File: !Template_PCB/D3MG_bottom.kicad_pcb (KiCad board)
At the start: 2 copper layers, 50 x 86.5 mm, 0 parts

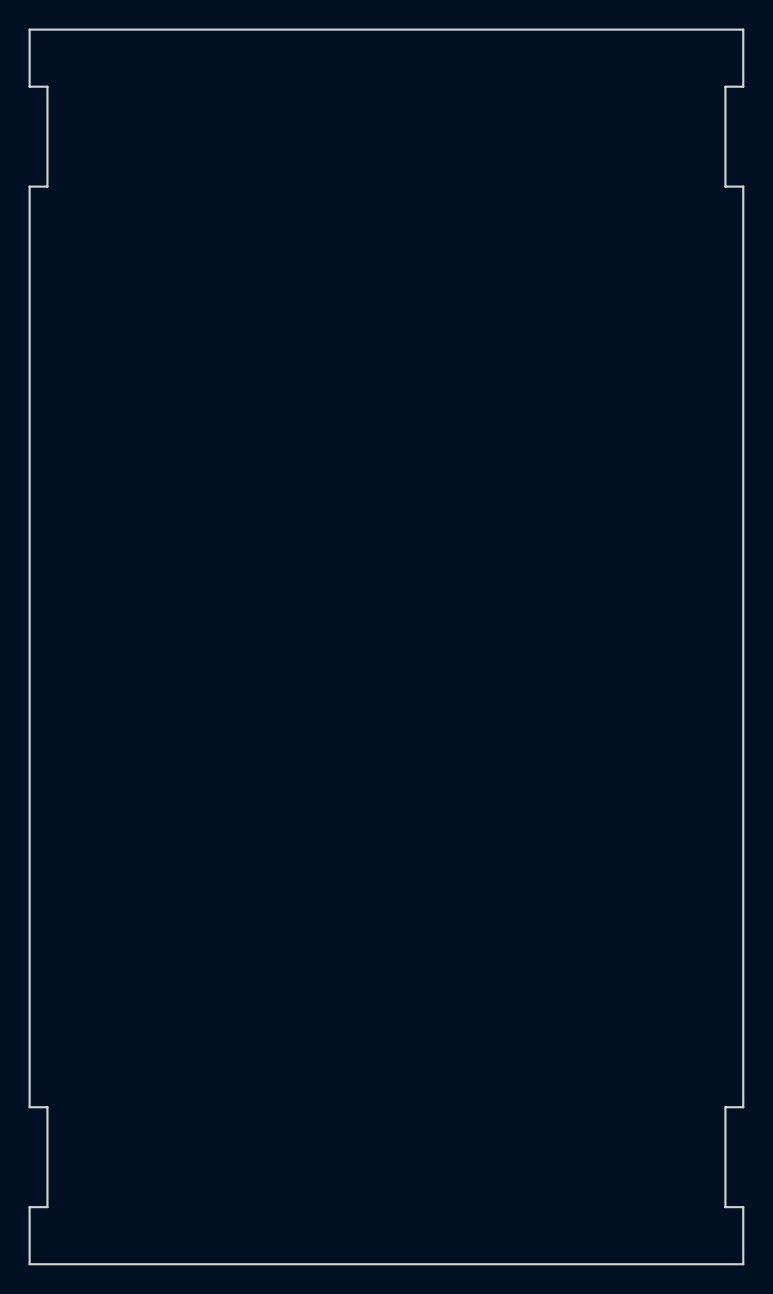
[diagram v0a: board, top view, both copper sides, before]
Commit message: + Spruce_60x70 Template_PCB
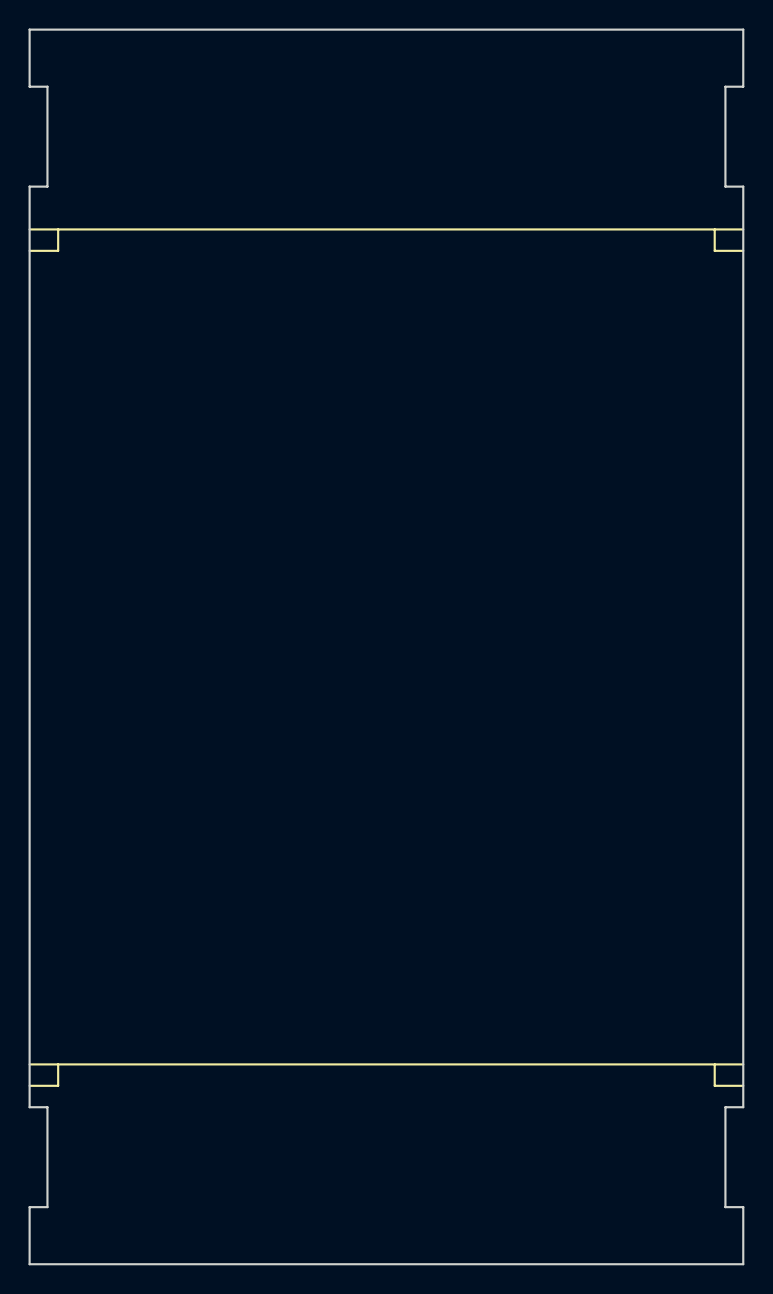
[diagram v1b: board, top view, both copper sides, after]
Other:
- board text removed: "bottom"
- board text removed: "top"
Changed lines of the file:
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@@
     (area 99.924999 49.924999 150.075001 136.575001)
     (thickness 1.6)
-    (drawings 35)
+    (drawings 33)
     (tracks 0)
     (zones 0)
@@
     (uvia_drill 0.3)
   )
-  (gr_text top (at 104 65) (layer Dwgs.User)
-    (effects (font (size 1.5 1.5) (thickness 0.3)))
-  )
-  (gr_text bottom (at 147.5 75.5 90) (layer Dwgs.User)
-    (effects (font (size 1.5 1.5) (thickness 0.3)))
-  )
-  (gr_line (start 102 65.5) (end 102 64) (angle 90) (layer Dwgs.User) (width 0.15))
-  (gr_line (start 100 65.5) (end 102 65.5) (angle 90) (layer Dwgs.User) (width 0.15))
-  (gr_line (start 148.5 50) (end 148.5 136.5) (angle 90) (layer Dwgs.User) (width 0.15))
-  (gr_line (start 148 65.5) (end 150 65.5) (angle 90) (layer Dwgs.User) (width 0.15))
-  (gr_line (start 148 64) (end 148 65.5) (angle 90) (layer Dwgs.User) (width 0.15))
-  (gr_line (start 100 64) (end 150 64) (angle 90) (layer Dwgs.User) (width 0.15))
-  (gr_line (start 101.5 136.5) (end 101.5 50) (angle 90) (layer Dwgs.User) (width 0.15))
-  (gr_line (start 102 124) (end 102 122.5) (angle 90) (layer Dwgs.User) (width 0.15))
-  (gr_line (start 100 124) (end 102 124) (angle 90) (layer Dwgs.User) (width 0.15))
-  (gr_line (start 148 124) (end 148 122.5) (angle 90) (layer Dwgs.User) (width 0.15))
-  (gr_line (start 150 124) (end 148 124) (angle 90) (layer Dwgs.User) (width 0.15))
-  (gr_line (start 100 122.5) (end 150 122.5) (angle 90) (layer Dwgs.User) (width 0.15))
+  (gr_line (start 102 65.5) (end 102 64) (angle 90) (layer F.SilkS) (width 0.15))
+  (gr_line (start 100 65.5) (end 102 65.5) (angle 90) (layer F.SilkS) (width 0.15))
+  (gr_line (start 148.5 50) (end 148.5 136.5) (angle 90) (layer B.SilkS) (width 0.15))
+  (gr_line (start 148 65.5) (end 150 65.5) (angle 90) (layer F.SilkS) (width 0.15))
+  (gr_line (start 148 64) (end 148 65.5) (angle 90) (layer F.SilkS) (width 0.15))
+  (gr_line (start 100 64) (end 150 64) (angle 90) (layer F.SilkS) (width 0.15))
+  (gr_line (start 101.5 136.5) (end 101.5 50) (angle 90) (layer B.SilkS) (width 0.15))
+  (gr_line (start 102 124) (end 102 122.5) (angle 90) (layer F.SilkS) (width 0.15))
+  (gr_line (start 100 124) (end 102 124) (angle 90) (layer F.SilkS) (width 0.15))
+  (gr_line (start 148 124) (end 148 122.5) (angle 90) (layer F.SilkS) (width 0.15))
+  (gr_line (start 150 124) (end 148 124) (angle 90) (layer F.SilkS) (width 0.15))
+  (gr_line (start 100 122.5) (end 150 122.5) (angle 90) (layer F.SilkS) (width 0.15))
   (gr_line (start 150 93.25) (end 100 93.25) (angle 90) (layer Dwgs.User) (width 0.15))
   (gr_line (start 150 125.5) (end 148.75 125.5) (angle 90) (layer Edge.Cuts) (width 0.15))

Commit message: .
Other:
- net class wide wide added: clearance 0.2, trace_width 1, via_dia 0.9, via_drill 0.4
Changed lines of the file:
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@@
+    (uvia_drill 0.3)
+  )
+  (net_class "wide wide" ""
+    (clearance 0.2)
+    (trace_width 1)
+    (via_dia 0.9)
+    (via_drill 0.4)
+    (uvia_dia 0.7)
     (uvia_drill 0.3)
   )
